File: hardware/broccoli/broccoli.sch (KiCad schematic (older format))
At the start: 82 parts, among them J1 PCB Antenna, J2 USB-MICRO-B, P1 DIGITAL, P11 SCLK, P12 SDAT, P2 PROGRAM, P3 JTAG, P4 EXPAND, P5 ANALOG, P6 VCC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

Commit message: proper BAW56 symbol/module
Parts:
- removed D16: DIODE, symbol DIODE
- added D16: BAW56, symbol BAW56
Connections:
- net VCC: now also D16.2 (K2)
- net at C29.1, Q2.G, R1.2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: now also D16.3 (A)
- no-connect marks 11 -> 12

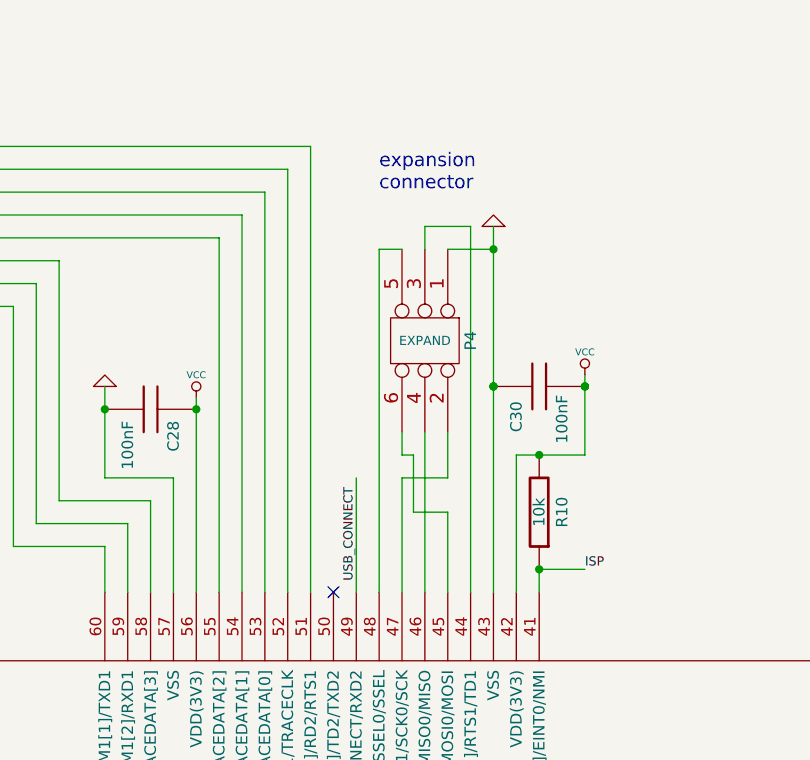
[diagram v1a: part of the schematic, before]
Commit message: Broccoli: added button, tweaked component placement
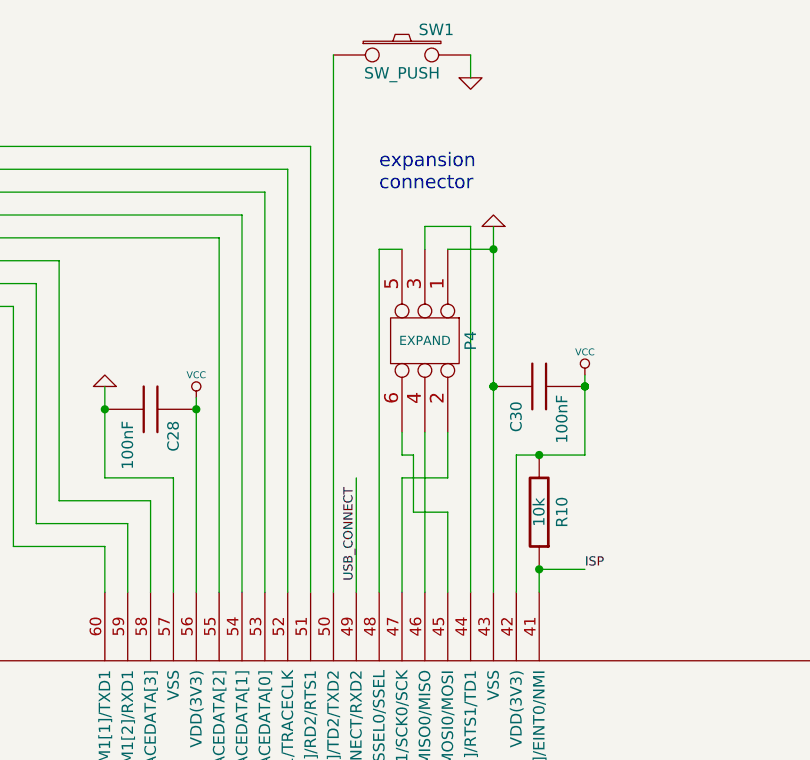
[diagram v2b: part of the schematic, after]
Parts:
- added SW1: SW_PUSH, symbol SW_PUSH
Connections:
- net GND: now also SW1.2
- net at U4.50 (P2[8]/TD2/TXD2): now also SW1.1
- no-connect marks 12 -> 11
